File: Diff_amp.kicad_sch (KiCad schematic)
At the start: 5 parts, among them Q1 NMOS, Q2 NMOS

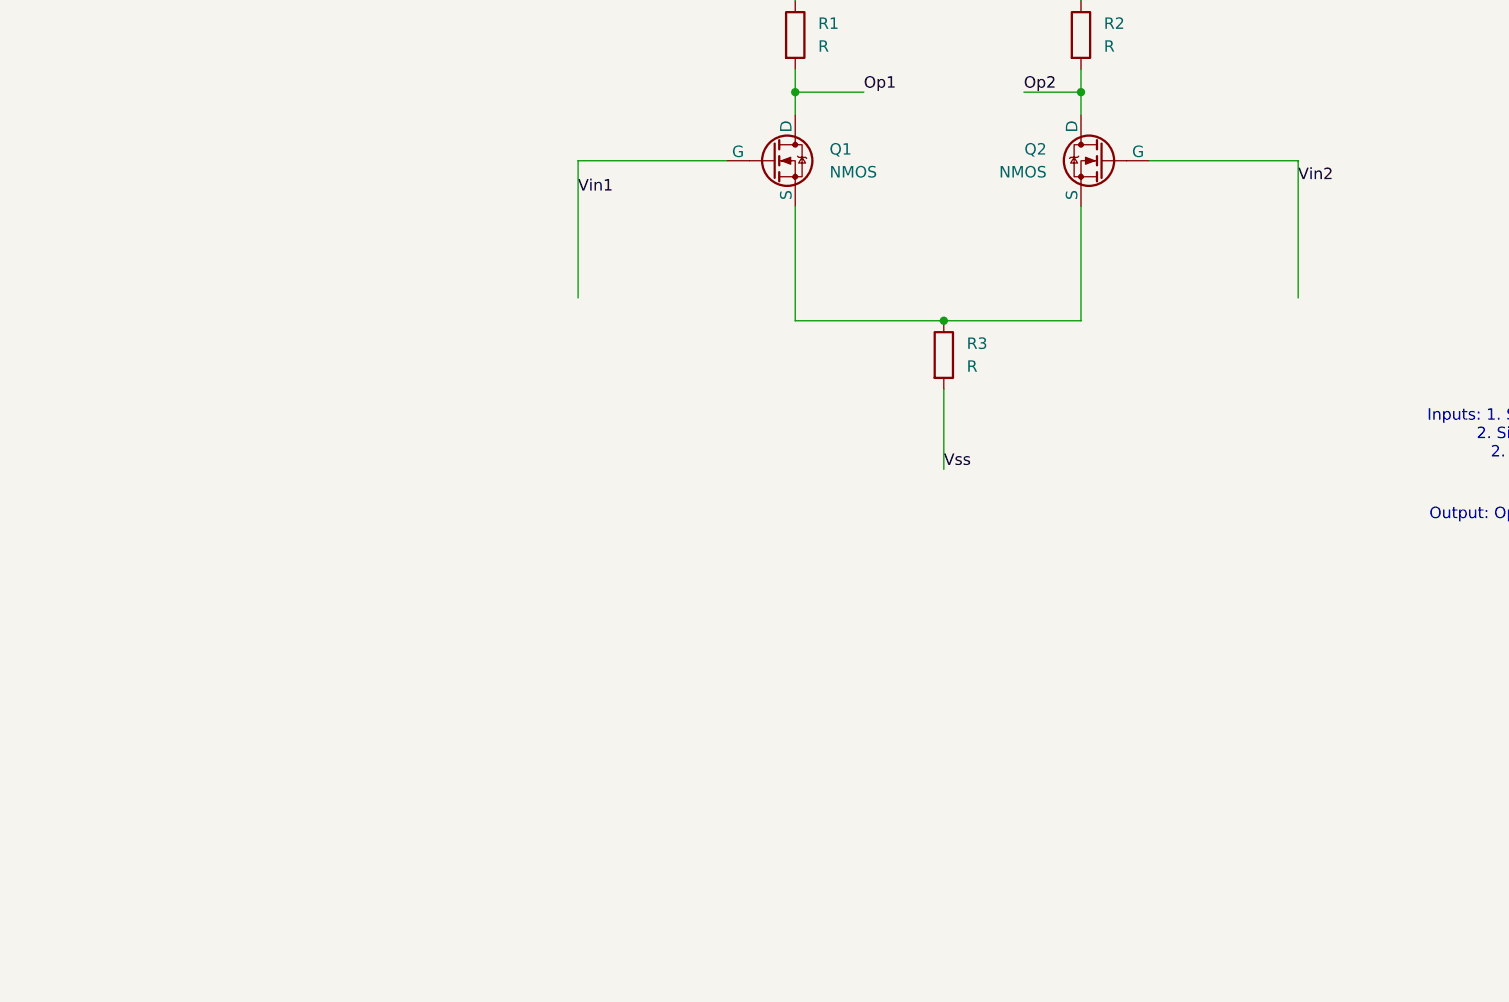
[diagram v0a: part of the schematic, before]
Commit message: Added Input Connectors
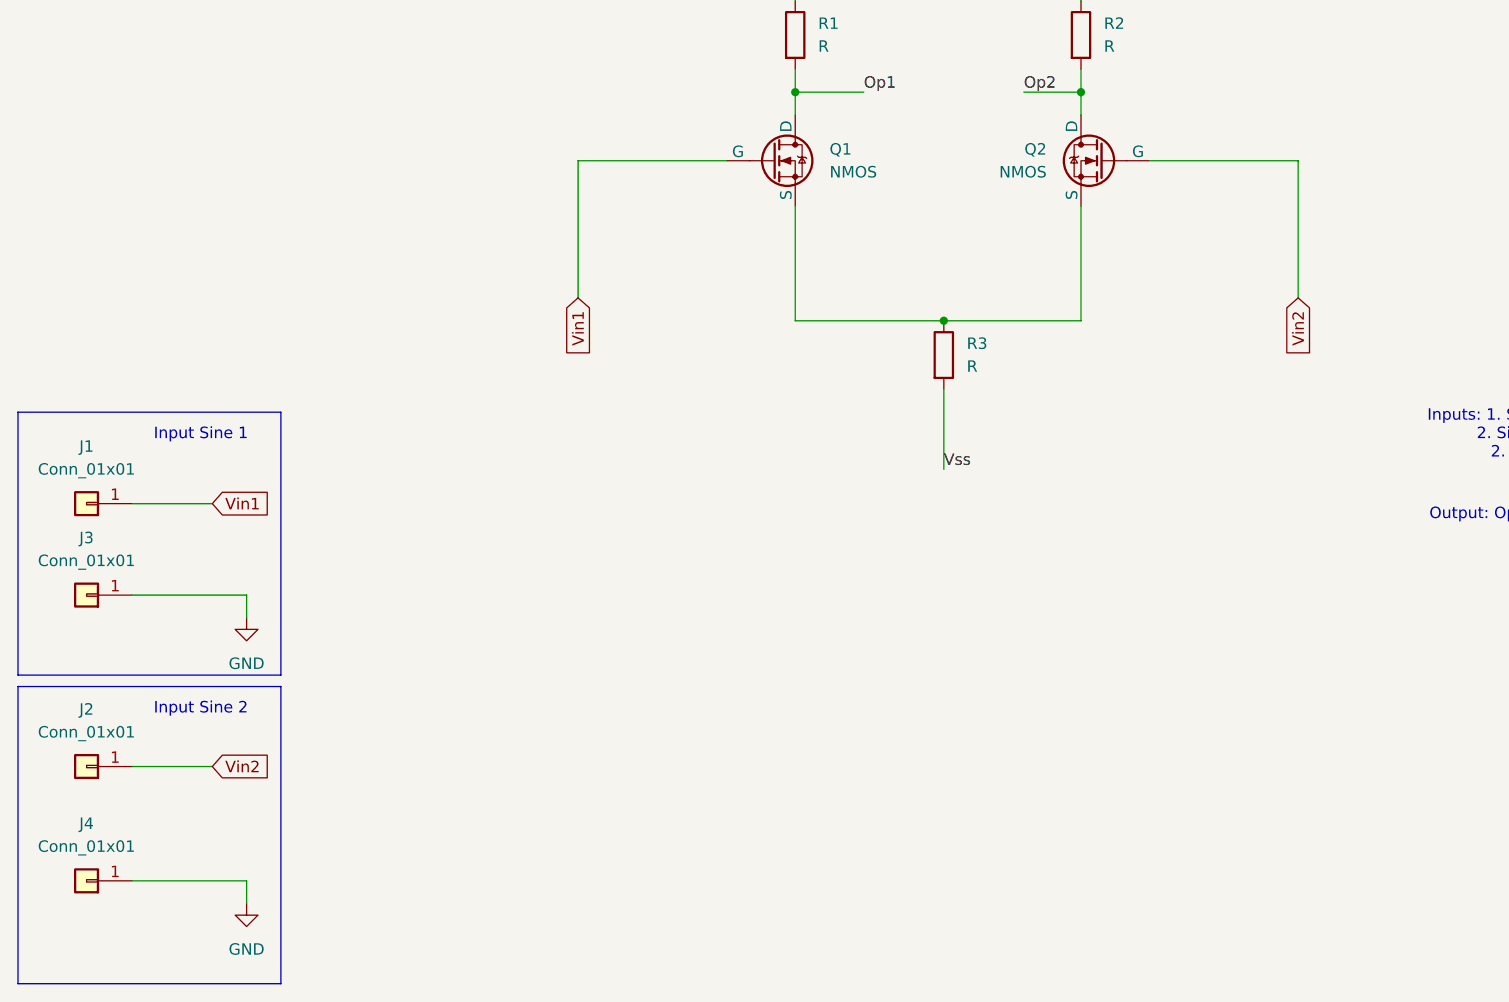
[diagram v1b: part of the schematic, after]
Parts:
- added J1, J2, J3, J4: Conn_01x01, Connector_PinHeader_2.54mm:PinHeader_1x01_P2.54mm_Vertical, symbol Connector_Generic:Conn_01x01
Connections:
- net Vin1: now also J1.1 (Pin_1)
- net Vin2: now also J2.1 (Pin_1)
- new net GND: J3.1 (Pin_1), J4.1 (Pin_1)
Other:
- note added: "Input Sine 1"
- note added: "Input Sine 2"

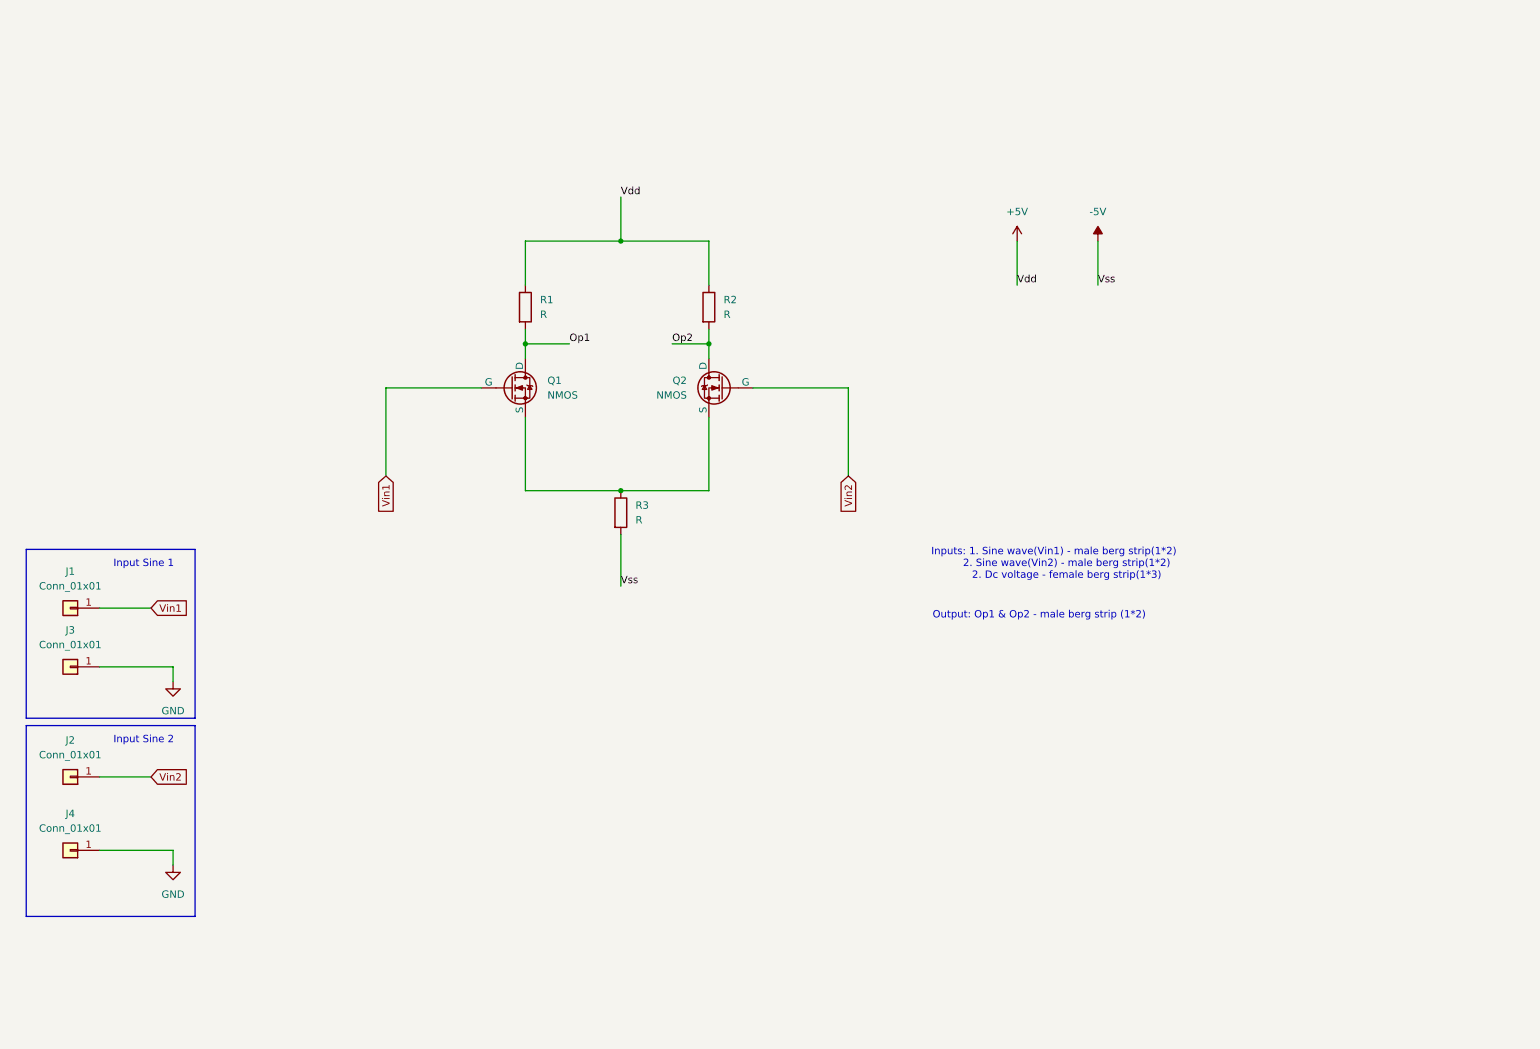
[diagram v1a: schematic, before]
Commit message: Added connectors for DC voltage
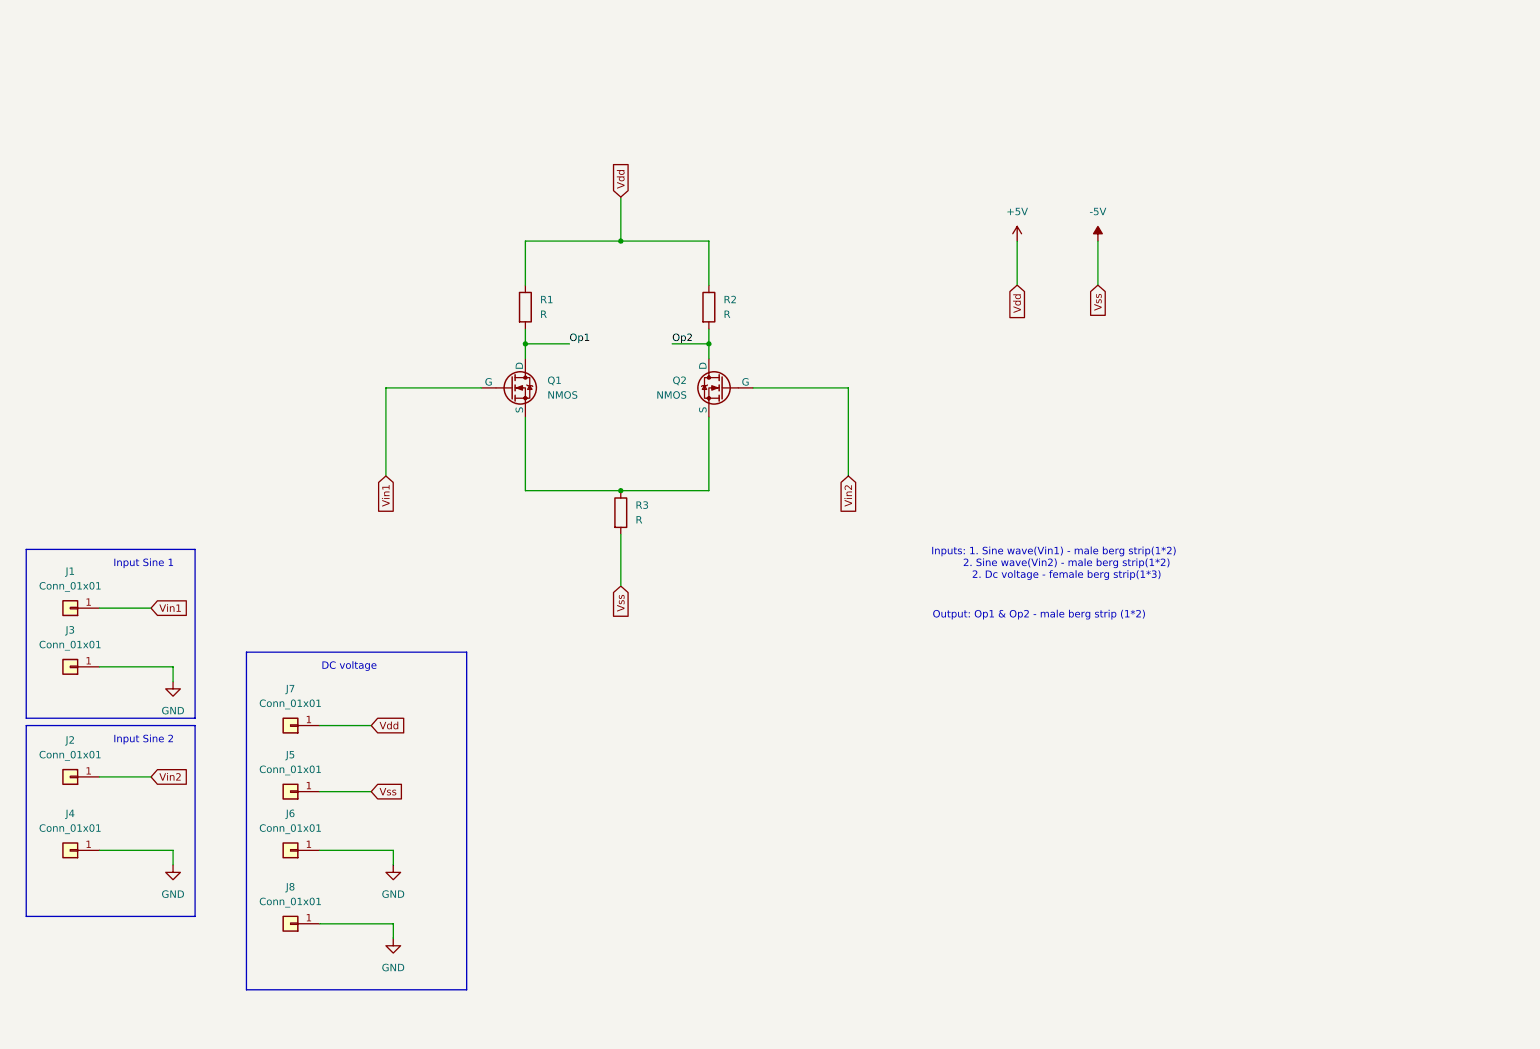
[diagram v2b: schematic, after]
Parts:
- added J5, J6, J7, J8: Conn_01x01, Connector_PinHeader_2.54mm:PinHeader_1x01_P2.54mm_Vertical, symbol Connector_Generic:Conn_01x01
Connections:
- net +5V: now also J7.1 (Pin_1)
- net -5V: now also J5.1 (Pin_1)
- net GND: now also J6.1 (Pin_1), J8.1 (Pin_1)
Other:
- note added: "DC voltage"

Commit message: Added output connectors
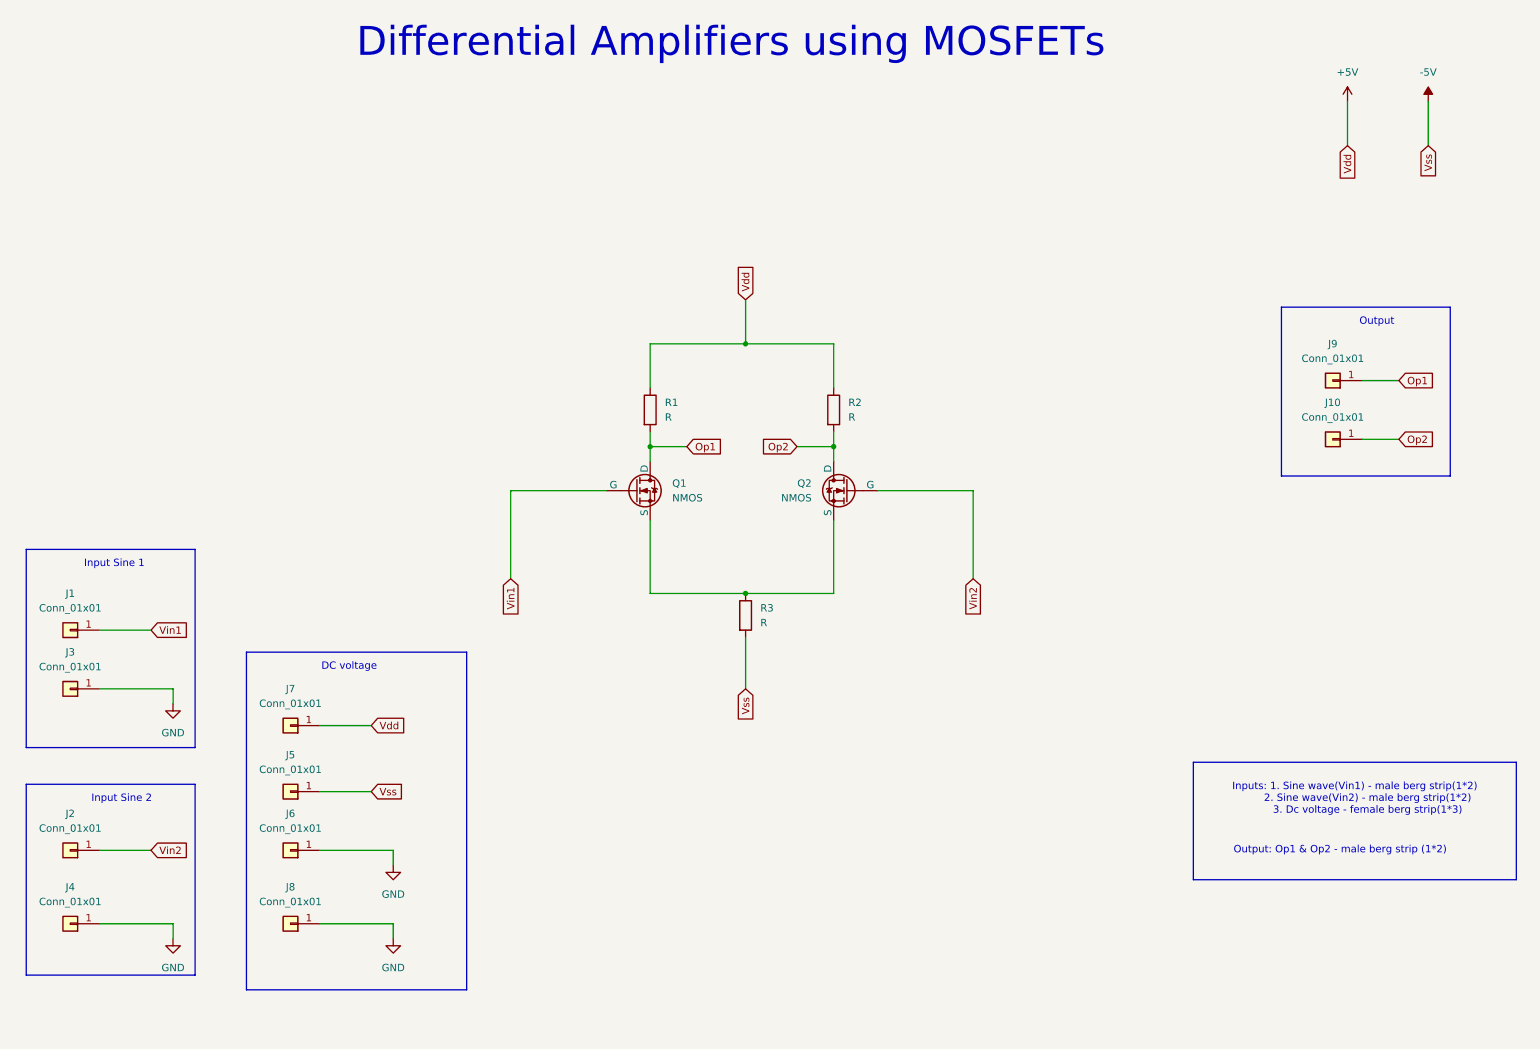
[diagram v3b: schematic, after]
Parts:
- added J10, J9: Conn_01x01, Connector_PinHeader_2.54mm:PinHeader_1x01_P2.54mm_Vertical, symbol Connector_Generic:Conn_01x01
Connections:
- net Op1: now also J9.1 (Pin_1)
- net Op2: now also J10.1 (Pin_1)
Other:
- note added: "Differential Amplifiers using MOSFETs"
- note added: "Inputs: 1. Sine wave(Vin1) - male berg strip(1*2) 2. Sine wave(Vin2) - male berg strip(1*2) 3. Dc voltage - female berg strip(1*3)"
- note added: "Output"
- note removed: "Inputs: 1. Sine wave(Vin1) - male berg strip(1*2) 2. Sine wave(Vin2) - male berg strip(1*2) 2. Dc voltage - female berg strip(1*3)"
- moved on the sheet: J1, J2, J3, J4, Q1, Q2, R1, R2, R3

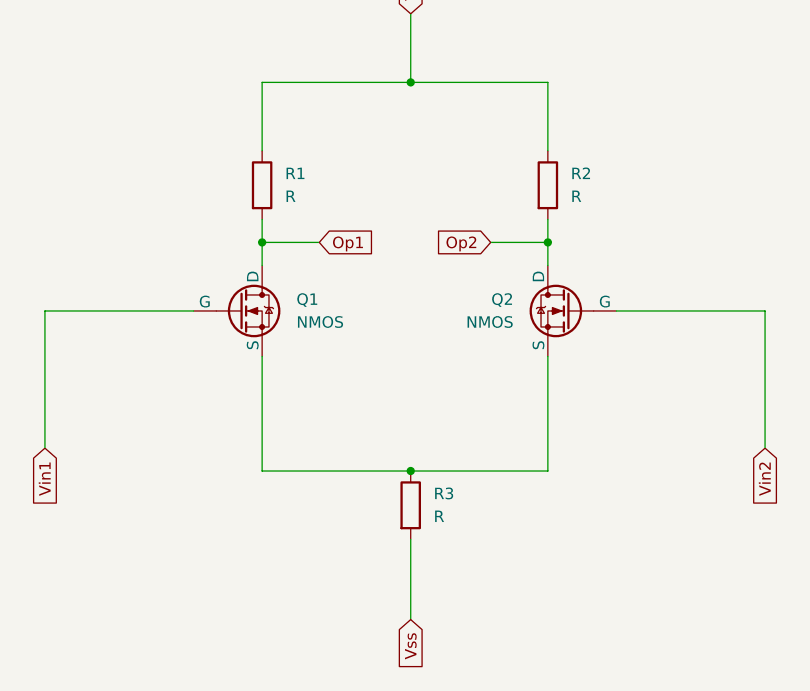
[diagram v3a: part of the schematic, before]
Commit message: Assigned footprints
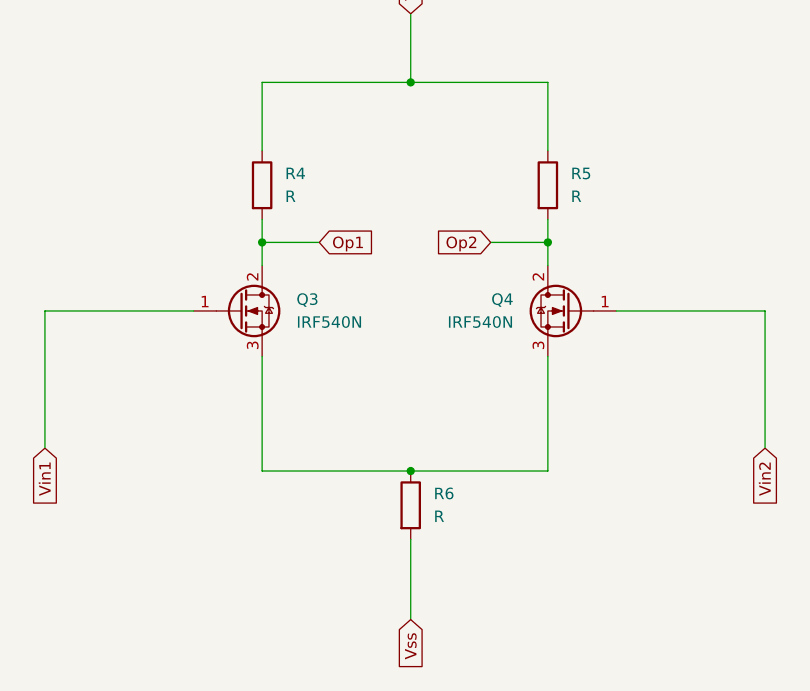
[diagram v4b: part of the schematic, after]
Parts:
- removed Q1, Q2: NMOS, symbol Simulation_SPICE:NMOS
- removed R1, R2, R3: R, symbol Device:R
- added Q3, Q4: IRF540N, Package_TO_SOT_THT:TO-220-3_Vertical, symbol Transistor_FET:IRF540N
- added R4, R5, R6: R, Resistor_THT:R_Axial_DIN0309_L9.0mm_D3.2mm_P15.24mm_Horizontal, symbol Device:R
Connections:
- net +5V: now also R4.1, R5.1
- net -5V: now also R6.2
- net Op1: now also Q3.2 (D), R4.2
- net Op2: now also Q4.2 (D), R5.2
- net Vin1: now also Q3.1 (G)
- net Vin2: now also Q4.1 (G)
- new net: Q3.3 (S), Q4.3 (S), R6.1
